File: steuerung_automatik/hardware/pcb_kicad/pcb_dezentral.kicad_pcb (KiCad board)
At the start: 2 copper layers, 55 x 73.5 mm, 92 parts, among them J1 weidmueller_SL5.08HC-06-90, J2 weidmueller_SL5.08HC-10-90, J901 USB_C_Receptacle_USB2.0, Q1 AO3400A, SW1 dip_switch_SPST16, SW901 SW_MEC_5E, U1 SP3485EN-L/TR, U2 AOZ1282CI, U901 RP2040, U902 AMS1117-3.3, U903 W25Q128JVS, Y901 Crystal_GND24_Small

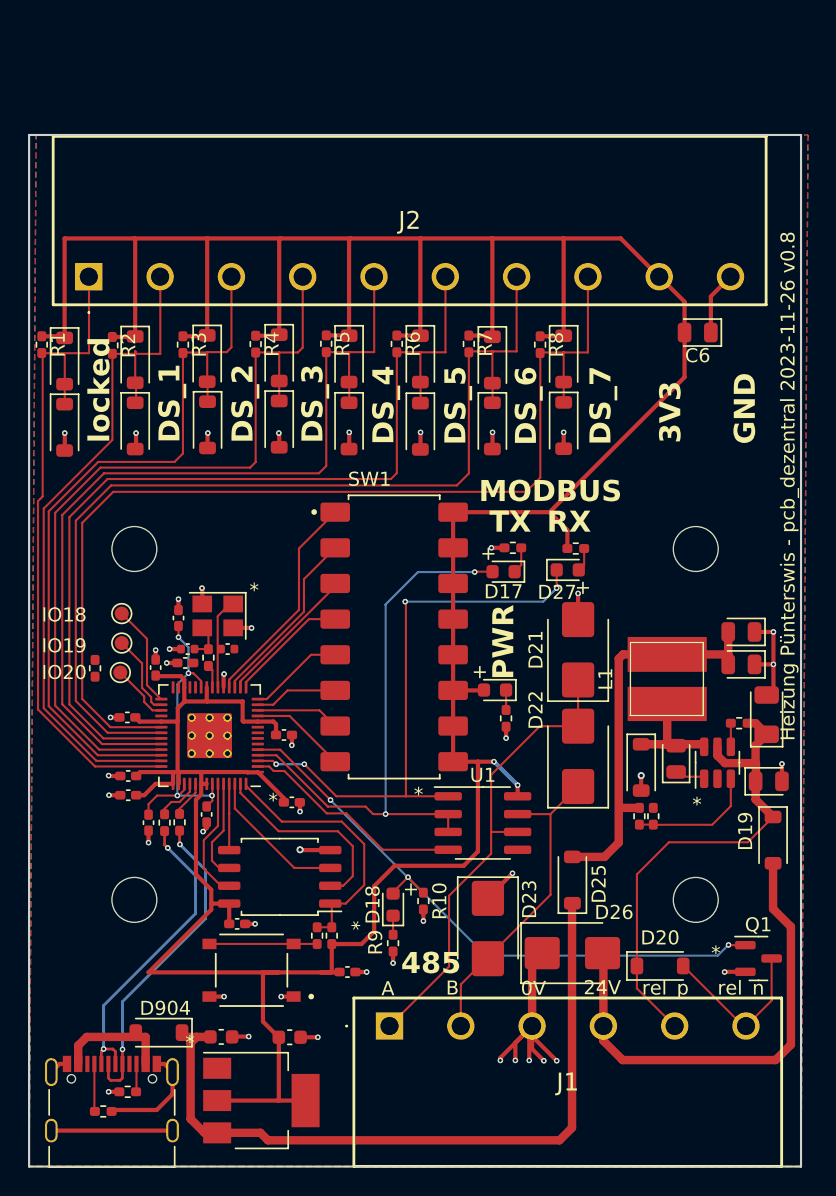
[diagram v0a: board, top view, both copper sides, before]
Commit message: Feedback JLCPCB, v0.81
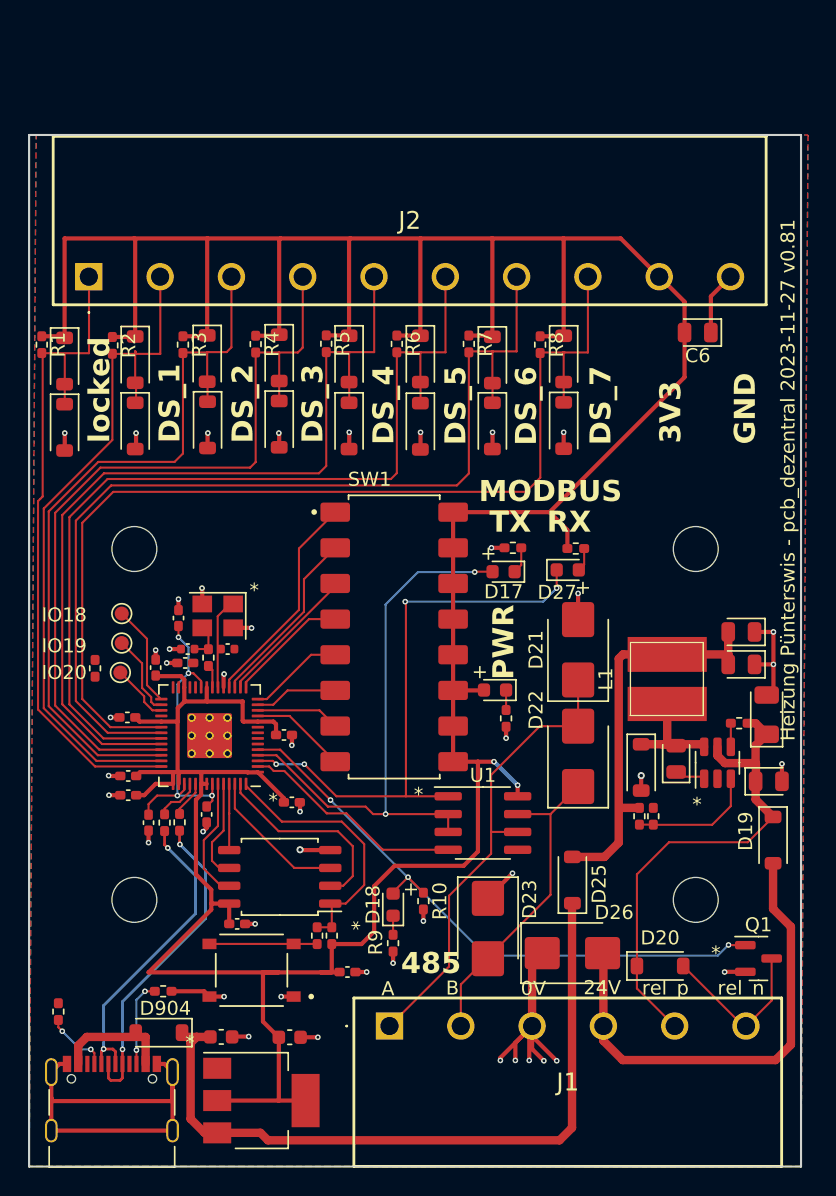
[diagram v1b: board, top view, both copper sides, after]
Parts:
- moved R901 7.80 mm to (76.1, 121.5), turned to 90 degrees
- moved R902 7.60 mm to (83.6, 120.0), turned to 0 degrees
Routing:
- net GND: track 89.2 -> 104.3 mm, vias 46 -> 45
- net Net-(J901-CC2): track 1.96 -> 6.13 mm, vias 0 -> 2
- net Net-(J901-CC1): track 3.35 -> 4.63 mm, vias 0 -> 2

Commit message: pcb_dezentral v1.0
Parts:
- added C7: 100n 50V, Diode_SMD:D_0805_2012Metric, F.Cu at (107.9, 102.3)
- added D28: LED WHITE, 00_project_library:LED_0603_1608Metric, F.Cu at (89.3, 87.6)
- added R17: 4k7, Resistor_SMD:R_0402_1005Metric_Pad0.72x0.64mm_HandSolder, F.Cu at (109.5, 104.0)
- added R18: 10k, Resistor_SMD:R_0402_1005Metric_Pad0.72x0.64mm_HandSolder, F.Cu at (95.2, 122.9)
- added R19: 10k, Resistor_SMD:R_0402_1005Metric_Pad0.72x0.64mm_HandSolder, F.Cu at (113.0, 108.3)
- added R20: 470R, Resistor_SMD:R_0402_1005Metric_Pad0.72x0.64mm_HandSolder, F.Cu at (91.6, 86.8)
- moved R14 24.2 mm to (100.2, 108.0)
- moved D901 4.30 mm to (106.6, 94.3), turned to 90 degrees
- moved R905 3.68 mm to (106.6, 97.1)
- moved C908 0.43 mm to (84.7, 96.6), turned to 0 degrees
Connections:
- net 485_A renamed 485_D+
- net 485_B renamed 485_D-
- R906 pad 1: Net-(SW901-A) -> button
- SW901 pad 3: Net-(SW901-A) -> button
- SW901 pad 4: Net-(SW901-A) -> button
- U901 pad 6: unconnected-(U901-GPIO4-Pad6) -> button
- U901 pad 8: unconnected-(U901-GPIO6-Pad8) -> ZENTRALE_LED
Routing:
- net button: track 0.00 -> 22.9 mm, vias 0 -> 2
- net ZENTRALE_LED: track 0.00 -> 14.2 mm, vias 0 -> 2
- net +5V: track 52.3 -> 60.2 mm
- net Net-(SW901-A): track 7.66 -> 0.00 mm
- net 485_D+: track 33.7 -> 39.8 mm
- net 485_D-: track 22.9 -> 27.1 mm
- net GND: track 104.3 -> 100.8 mm, vias 45 -> 42
- net Net-(C7-Pad1): track 0.00 -> 1.75 mm
- net Net-(D28-K): track 0.00 -> 1.70 mm
- net +3V3: track 282.5 -> 283.6 mm
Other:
- board text added: "D+"
- board text added: "D-"
- board text added: "ZENTRALE"
- board text removed: "A"
- board text removed: "B"
